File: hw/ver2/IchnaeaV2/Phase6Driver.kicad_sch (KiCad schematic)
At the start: 21 parts, among them Q2 MCAC80N10Y, Q3 MCAC80N10Y, Q4 MCAC80N10Y, Q5 MCAC80N10Y, U2 HIP2210

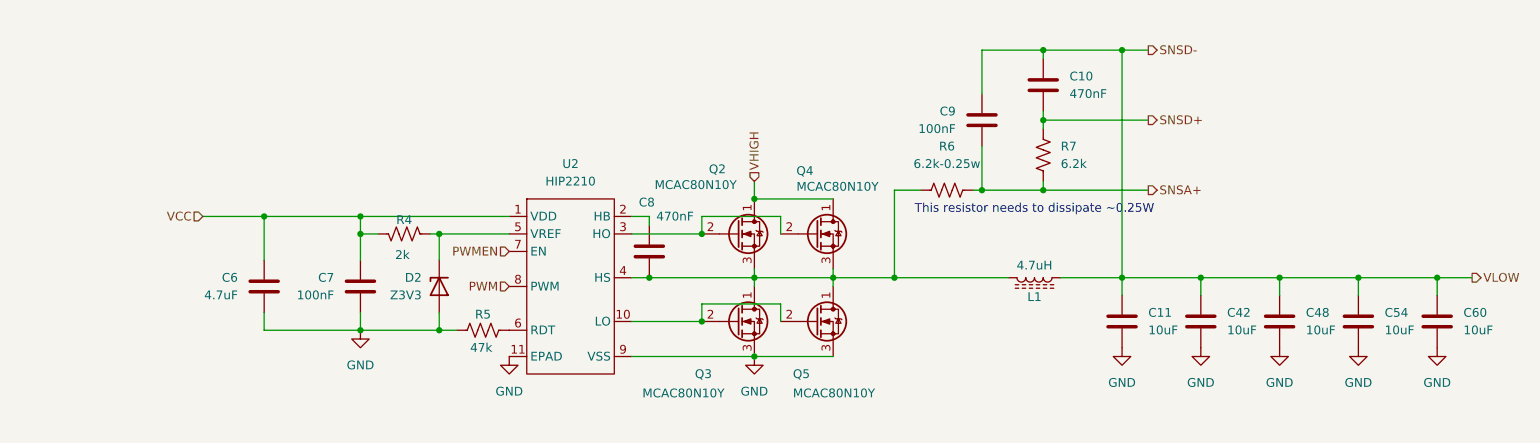
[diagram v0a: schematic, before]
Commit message: Trying to further compress power loop area
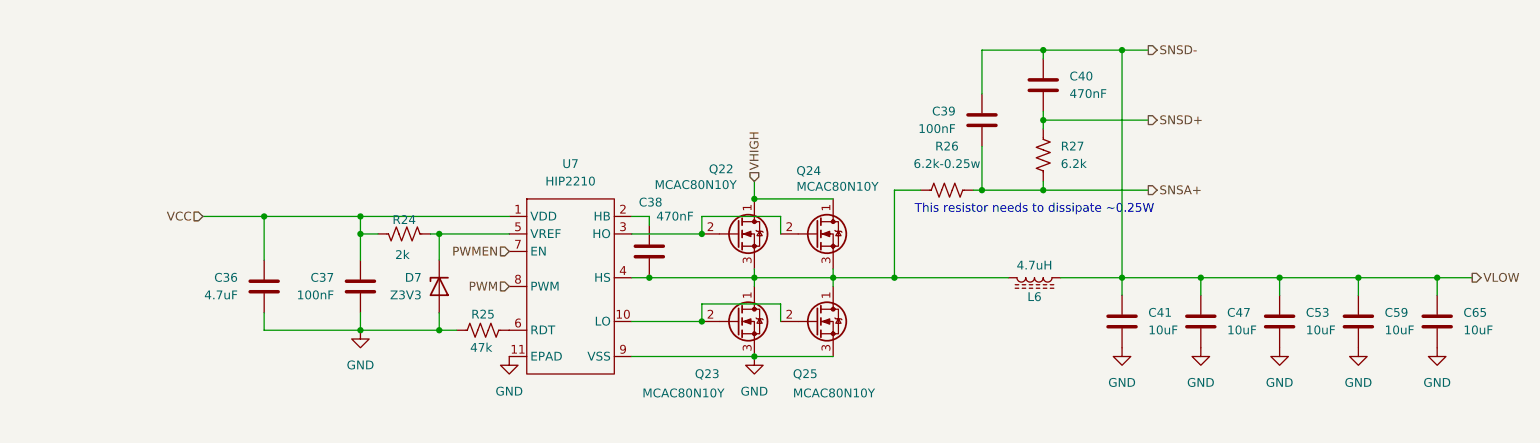
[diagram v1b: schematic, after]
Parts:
- renumbered C6 to C36, C7 to C37, C8 to C38, C9 to C39, C10 to C40, C11 to C41, C42 to C47, C48 to C53, C54 to C59, C60 to C65, D2 to D7, L1 to L6, Q2 to Q22, Q3 to Q23, Q4 to Q24, Q5 to Q25, R4 to R24, R5 to R25, R6 to R26, R7 to R27, U2 to U7

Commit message: Not quite happy with the power stage just yet.
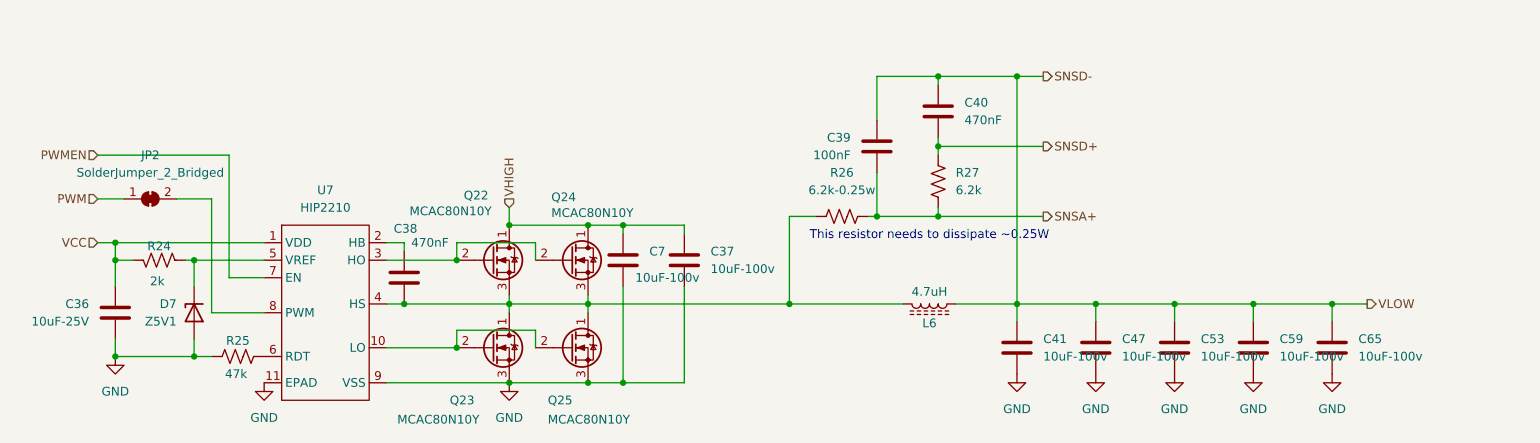
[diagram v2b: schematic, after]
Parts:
- added C7: 10uF-100v, Capacitor_SMD:C_1210_3225Metric_Pad1.33x2.70mm_HandSolder, symbol Device:C
- added JP2: SolderJumper_2_Bridged, Jumper:SolderJumper-2_P1.3mm_Bridged_Pad1.0x1.5mm, symbol Jumper:SolderJumper_2_Bridged
- C36: value 4.7uF -> 10uF-25V; LCSC C19666 -> C96446
- C37: value 100nF -> 10uF-100v; footprint Capacitor_SMD:C_0603_1608Metric -> Capacitor_SMD:C_1210_3225Metric_Pad1.33x2.70mm_HandSolder; Digikey N/A -> 445-CGA6P1X7R1N106M250ACCT-ND; LCSC C14663 -> C576517
- C41, C47, C53, C59, C65: value 10uF -> 10uF-100v
- D7: value Z3V3 -> Z5V1; LCSC C5353025 -> C2903912
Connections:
- net GND: now also C7.2
- net PWM: now also JP2.1 (A); no longer U7.8 (PWM)
- net VCC: no longer C37.1
- net VHIGH: now also C37.1, C7.1
- new net: JP2.2 (B), U7.8 (PWM)
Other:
- moved on the sheet: C36, C38, C39, C40, C41, C47, C53, C59, C65, D7, L6, Q22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

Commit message: Sync work to main PC
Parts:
- removed D7: Z5V1, Diode_SMD:D_SOD-123, symbol Device:D_Zener
- removed JP2: SolderJumper_2_Bridged, Jumper:SolderJumper-2_P1.3mm_Bridged_Pad1.0x1.5mm, symbol Jumper:SolderJumper_2_Bridged
- added R54, R56: 0, Resistor_SMD:R_0603_1608Metric, symbol Device:R_US
- added R61: 10k, Resistor_SMD:R_0603_1608Metric, symbol Device:R_US
- R24: value 2k -> 6.2k; LCSC (none) -> C4260
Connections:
- net GND: now also R24.2
- net PWM: now also R54.2
- net PWMEN: now also R56.2; no longer U7.7 (EN)
- net SNSD-: now also L6.2; no longer L6.1
- net VCC: now also R61.1; no longer R24.2
- net at C38.2, Q22.3 (S), Q23.1 (D)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: now also L6.1; no longer L6.2
- net at R24.1, U7.5 (VREF): now also R61.2
- net at U7.8 (PWM): now also R54.1
- new net: R56.1, U7.7 (EN)
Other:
- moved on the sheet: L6

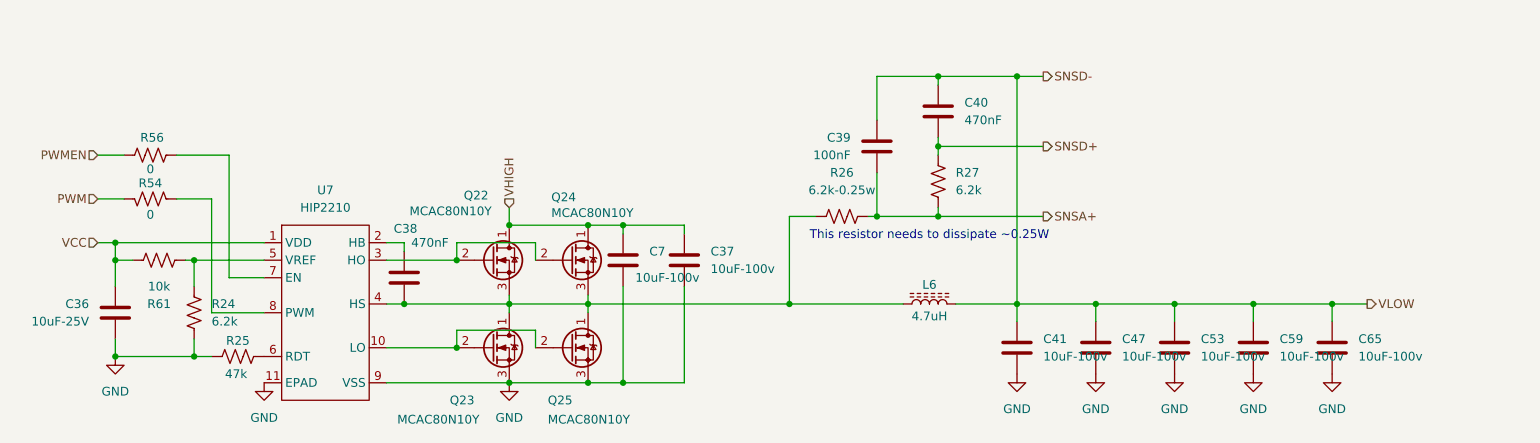
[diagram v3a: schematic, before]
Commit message: Partially work through the V1 notes. Start adding some of the control stage circuitry.
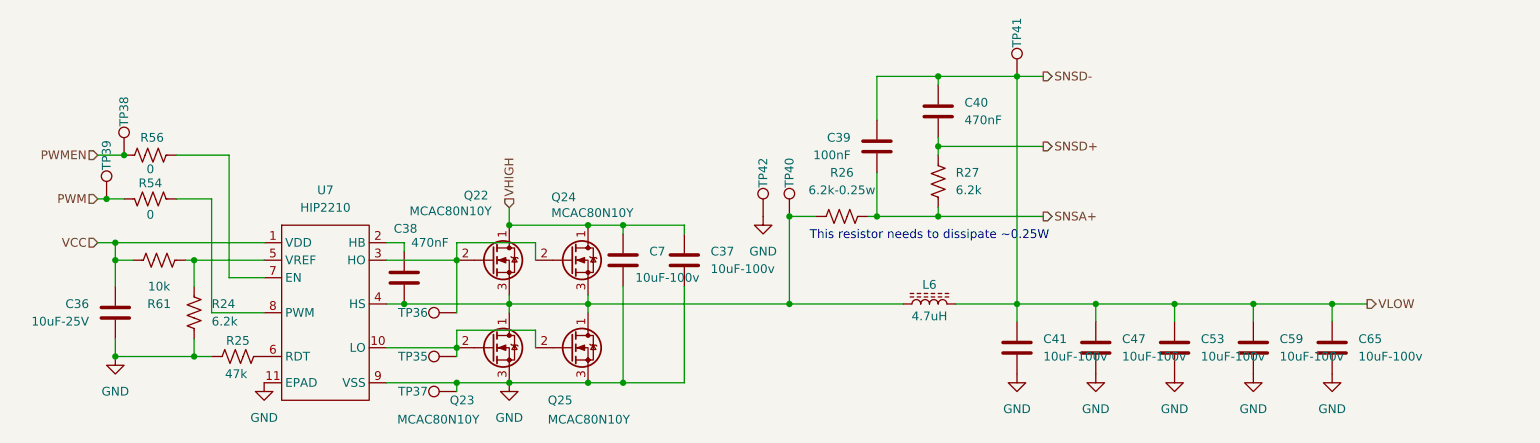
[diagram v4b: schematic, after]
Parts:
- added TP35, TP36, TP37, TP38, TP39, TP40, TP41, TP42: TestPoint, TestPoint:TestPoint_Pad_D1.0mm, symbol Connector:TestPoint
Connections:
- net GND: now also TP37.1, TP42.1
- net PWM: now also TP39.1
- net PWMEN: now also TP38.1
- net SNSD-: now also TP41.1
- net at C38.2, L6.1, Q22.3 (S)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: now also TP40.1
- net at Q23.2 (G), Q25.2 (G), U7.10 (LO): now also TP35.1
- net at Q22.2 (G), Q24.2 (G), U7.3 (HO): now also TP36.1

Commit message: Test production outputs for V2
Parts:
- R26: LCSC N/A -> C3017007
- TP35, TP36, TP37, TP38, TP39, TP40, TP41, TP42: LCSC (none) -> N/A
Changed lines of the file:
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@@
+			)
+		)
+		(property "LCSC" "N/A"
+			(at 200.66 66.04 0)
+			(effects
+				(font
+					(size 1.27 1.27)
+				)
+				(hide yes)
 			)
 		)
@@
 			)
 		)
+		(property "LCSC" "N/A"
+			(at 119.38 106.68 0)
+			(effects
+				(font
+					(size 1.27 1.27)
+				)
+				(hide yes)
+			)
+		)
 		(pin "1"
 		)
@@
 		)
 		(property "Description" "test point"
+			(at 163.83 86.36 0)
+			(effects
+				(font
+					(size 1.27 1.27)
+				)
+				(hide yes)
+			)
+		)
+		(property "LCSC" "N/A"
 			(at 163.83 86.36 0)
 			(effects
@@
 			)
 		)
+		(property "LCSC" "N/A"
+			(at 71.12 77.47 0)
+			(effects
+				(font
+					(size 1.27 1.27)
+				)
+				(hide yes)
+			)
+		)
 		(pin "1"
 		)
@@
 			)
 		)
+		(property "LCSC" "N/A"
+			(at 167.64 86.36 0)
+			(effects
+				(font
+					(size 1.27 1.27)
+				)
+				(hide yes)
+			)
+		)
 		(pin "1"
 		)
@@
 			)
 		)
+		(property "LCSC" "N/A"
+			(at 119.38 100.33 0)
+			(effects
+				(font
+					(size 1.27 1.27)
+				)
+				(hide yes)
+			)
+		)
 		(pin "1"
 		)
@@
 			)
 		)
-		(property "LCSC" "N/A"
+		(property "LCSC" "C3017007"
 			(at 175.26 86.36 0)
 			(effects
@@
 		)
 		(property "Description" "test point"
+			(at 68.58 83.82 0)
+			(effects
+				(font
+					(size 1.27 1.27)
+				)
+				(hide yes)
+			)
+		)
+		(property "LCSC" "N/A"
 			(at 68.58 83.82 0)
 			(effects
@@
 			(at 119.38 111.76 0)
 			(effects
+				(font
+					(size 1.27 1.27)
+				)
+				(hide yes)
+			)
+		)
+		(property "LCSC" "N/A"
+			(at 119.38 111.76 0)
+			(effects

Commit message: Sync schematic updates
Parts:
- R25: LCSC C21189 -> C25819
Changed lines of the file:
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@@
 			)
 		)
-		(property "LCSC" "C21189"
+		(property "LCSC" "C25819"
 			(at 87.63 106.68 0)
 			(effects
